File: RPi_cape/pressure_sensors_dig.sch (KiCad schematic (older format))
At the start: 11 parts, among them J17 Pressure_sensor_barb, J18 Pressure_sensor_barb, U10 MS5803-05BA, U14 BMP388

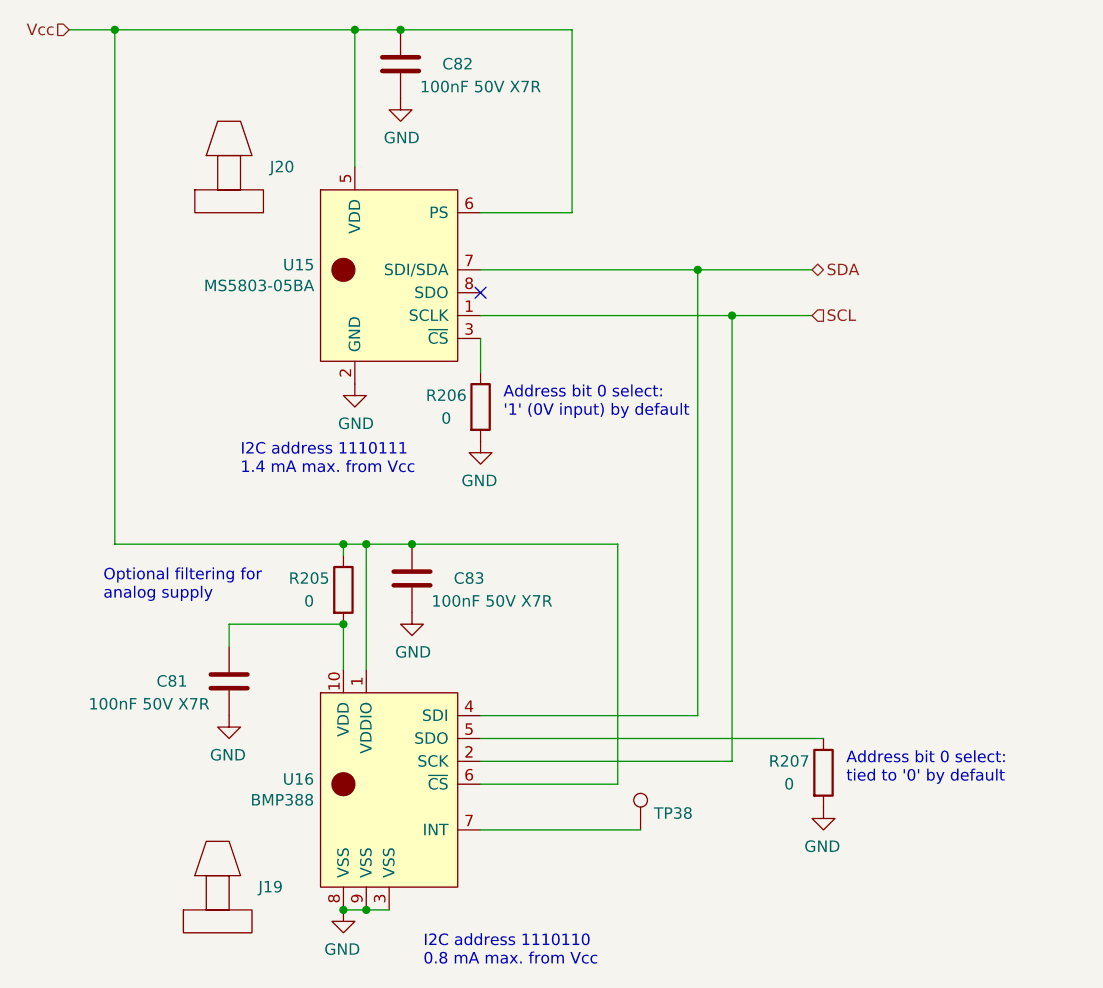
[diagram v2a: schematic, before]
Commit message: Admin (naming, license), improvements based on testing
Updated name on schematic, PCB silkscreen
Added 3 mounting holes on inside area of board for better mechanical robustness
Removed extra unused pressure sensor barb packages from library
Fixed Phoenix spring connector footprints, and added 3D models from Phoenix website
Added 3D models to TE encoder connector footprints, QFP-100 for CPLD, and 5019 testpoint
Changed DIAG_EN pin connection from valve drivers from +24V (too high) to +3.3V
Added CERN licensing terms
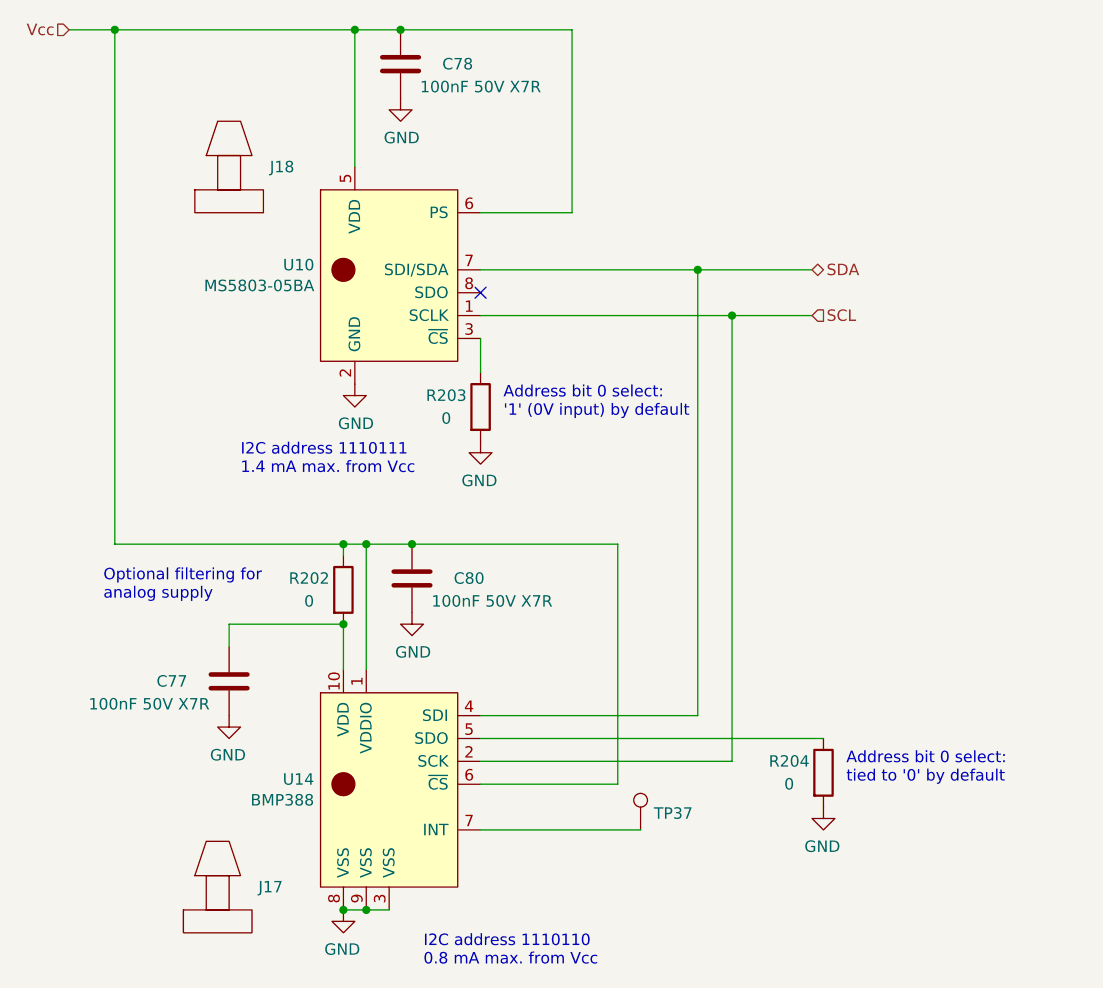
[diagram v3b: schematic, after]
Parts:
- J17, J18: footprint Ventilator:Pressure_sensor_barb_inner-lip-expanded-slots -> Ventilator:Pressure_sensor_barb
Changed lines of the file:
@@
 $Descr A4 11693 8268
 encoding utf-8
-Sheet 13 15
-Title "Raspberry Pi Hat for JamVent Adaptation"
+Sheet 12 15
+Title "GlobalVent Stand-Alone Controller"
 Date ""
-Rev "1.9"
-Comp "US JamVent Team"
-Comment1 "Don Straney"
-Comment2 ""
+Rev "1.10"
+Comp "US GlobalVent Team"
+Comment1 "Licensed under CERN-OHL-S v2"
+Comment2 "Don Straney"
 Comment3 ""
 Comment4 ""
@@
 AR Path="/5F518E26/5F542369" Ref="U10"  Part="1"
 AR Path="/5F593E41/5F542369" Ref="U15"  Part="1"
-F 0 "U15" H 2123 2821 50  0000 R CNN
+F 0 "U10" H 2123 2821 50  0000 R CNN
 F 1 "MS5803-05BA" H 2123 2730 50  0000 R CNN
 F 2 "Ventilator:TE_MS5803-05BA" H 2450 2800 50  0001 C CNN
@@
 AR Path="/5F518E26/5F542954" Ref="U14"  Part="1"
 AR Path="/5F593E41/5F542954" Ref="U16"  Part="1"
-F 0 "U16" H 2122 5071 50  0000 R CNN
+F 0 "U14" H 2122 5071 50  0000 R CNN
 F 1 "BMP388" H 2122 4980 50  0000 R CNN
 F 2 "Ventilator:Bosch_BMP388" H 2450 5100 50  0001 C CNN
@@
 AR Path="/5F518E26/5F5543A0" Ref="C77"  Part="1"
 AR Path="/5F593E41/5F5543A0" Ref="C81"  Part="1"
-F 0 "C81" H 1500 4600 50  0000 C CNN
+F 0 "C77" H 1500 4600 50  0000 C CNN
 F 1 "100nF 50V X7R" H 1400 4700 50  0000 C CNN
 F 2 "Capacitor_SMD:C_0603_1608Metric" H 1788 4450 50  0001 C CNN
@@
 AR Path="/5F518E26/5F5543B2" Ref="R202"  Part="1"
 AR Path="/5F593E41/5F5543B2" Ref="R205"  Part="1"
-F 0 "R205" H 2100 4250 50  0000 C CNN
+F 0 "R202" H 2100 4250 50  0000 C CNN
 F 1 "0" H 2100 4150 50  0000 C CNN
 F 2 "Resistor_SMD:R_1206_3216Metric" V 2180 4200 50  0001 C CNN
@@
 AR Path="/5F518E26/5F55CEFC" Ref="C80"  Part="1"
 AR Path="/5F593E41/5F55CEFC" Ref="C83"  Part="1"
-F 0 "C83" H 2300 4150 50  0000 C CNN
+F 0 "C80" H 2300 4150 50  0000 C CNN
 F 1 "100nF 50V X7R" H 2200 4250 50  0000 C CNN
 F 2 "Capacitor_SMD:C_0603_1608Metric" H 2588 4000 50  0001 C CNN
@@
 AR Path="/5F518E26/5F560E40" Ref="C78"  Part="1"
 AR Path="/5F593E41/5F560E40" Ref="C82"  Part="1"
-F 0 "C82" H 2250 1900 50  0000 C CNN
+F 0 "C78" H 2250 1900 50  0000 C CNN
 F 1 "100nF 50V X7R" H 2150 2000 50  0000 C CNN
 F 2 "Capacitor_SMD:C_0603_1608Metric" H 2538 1750 50  0001 C CNN
@@
 AR Path="/5F518E26/5F56BBEF" Ref="R204"  Part="1"
 AR Path="/5F593E41/5F56BBEF" Ref="R207"  Part="1"
-F 0 "R207" H 4200 5050 50  0000 C CNN
+F 0 "R204" H 4200 5050 50  0000 C CNN
 F 1 "0" H 4200 4950 50  0000 C CNN
 F 2 "Resistor_SMD:R_1206_3216Metric" V 4280 5000 50  0001 C CNN
@@
 AR Path="/5F518E26/5F570F1D" Ref="TP37"  Part="1"
 AR Path="/5F593E41/5F570F1D" Ref="TP38"  Part="1"
-F 0 "TP38" H 3608 5322 50  0000 L CNN
+F 0 "TP37" H 3608 5322 50  0000 L CNN
 F 1 "TestPoint" H 3608 5277 50  0001 L CNN
 F 2 "TestPoint:TestPoint_Pad_2.0x2.0mm" H 3750 5250 50  0001 C CNN
@@
 AR Path="/5F518E26/5F5769F4" Ref="R203"  Part="1"
 AR Path="/5F593E41/5F5769F4" Ref="R206"  Part="1"
-F 0 "R206" H 2700 3450 50  0000 C CNN
+F 0 "R203" H 2700 3450 50  0000 C CNN
 F 1 "0" H 2700 3350 50  0000 C CNN
 F 2 "Resistor_SMD:R_1206_3216Metric" V 2780 3400 50  0001 C CNN
@@
 AR Path="/5F518E26/5F666F01" Ref="J18"  Part="1"
 AR Path="/5F593E41/5F666F01" Ref="J20"  Part="1"
-F 0 "J20" H 1928 2650 50  0000 L CNN
+F 0 "J18" H 1928 2650 50  0000 L CNN
 F 1 "Pressure_sensor_barb" H 1700 2850 50  0001 C CNN
-F 2 "Ventilator:Pressure_sensor_barb_inner-lip-expanded-slots" H 1750 2500 50  0001 C CNN
+F 2 "Ventilator:Pressure_sensor_barb" H 1750 2500 50  0001 C CNN
 F 3 "" H 1750 2500 50  0001 C CNN
 	1    1750 2500
@@
 AR Path="/5F518E26/5F667549" Ref="J17"  Part="1"
 AR Path="/5F593E41/5F667549" Ref="J19"  Part="1"
-F 0 "J19" H 1878 5800 50  0000 L CNN
+F 0 "J17" H 1878 5800 50  0000 L CNN
 F 1 "Pressure_sensor_barb" H 1650 6000 50  0001 C CNN
-F 2 "Ventilator:Pressure_sensor_barb_inner-lip-expanded-slots" H 1700 5650 50  0001 C CNN
+F 2 "Ventilator:Pressure_sensor_barb" H 1700 5650 50  0001 C CNN
 F 3 "" H 1700 5650 50  0001 C CNN
 	1    1700 5650
